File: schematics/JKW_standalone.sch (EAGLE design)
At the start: 173 parts, among them IC1 4093D, IC2 AT-MEGA-8, IC4 ATMEGA2560-16AU, T1 Farnell: 1299313, T2 Farnell: 1299313, T3 Farnell: 1299313, T4 T-IRLMS6702, T5 Farnell: 1299313

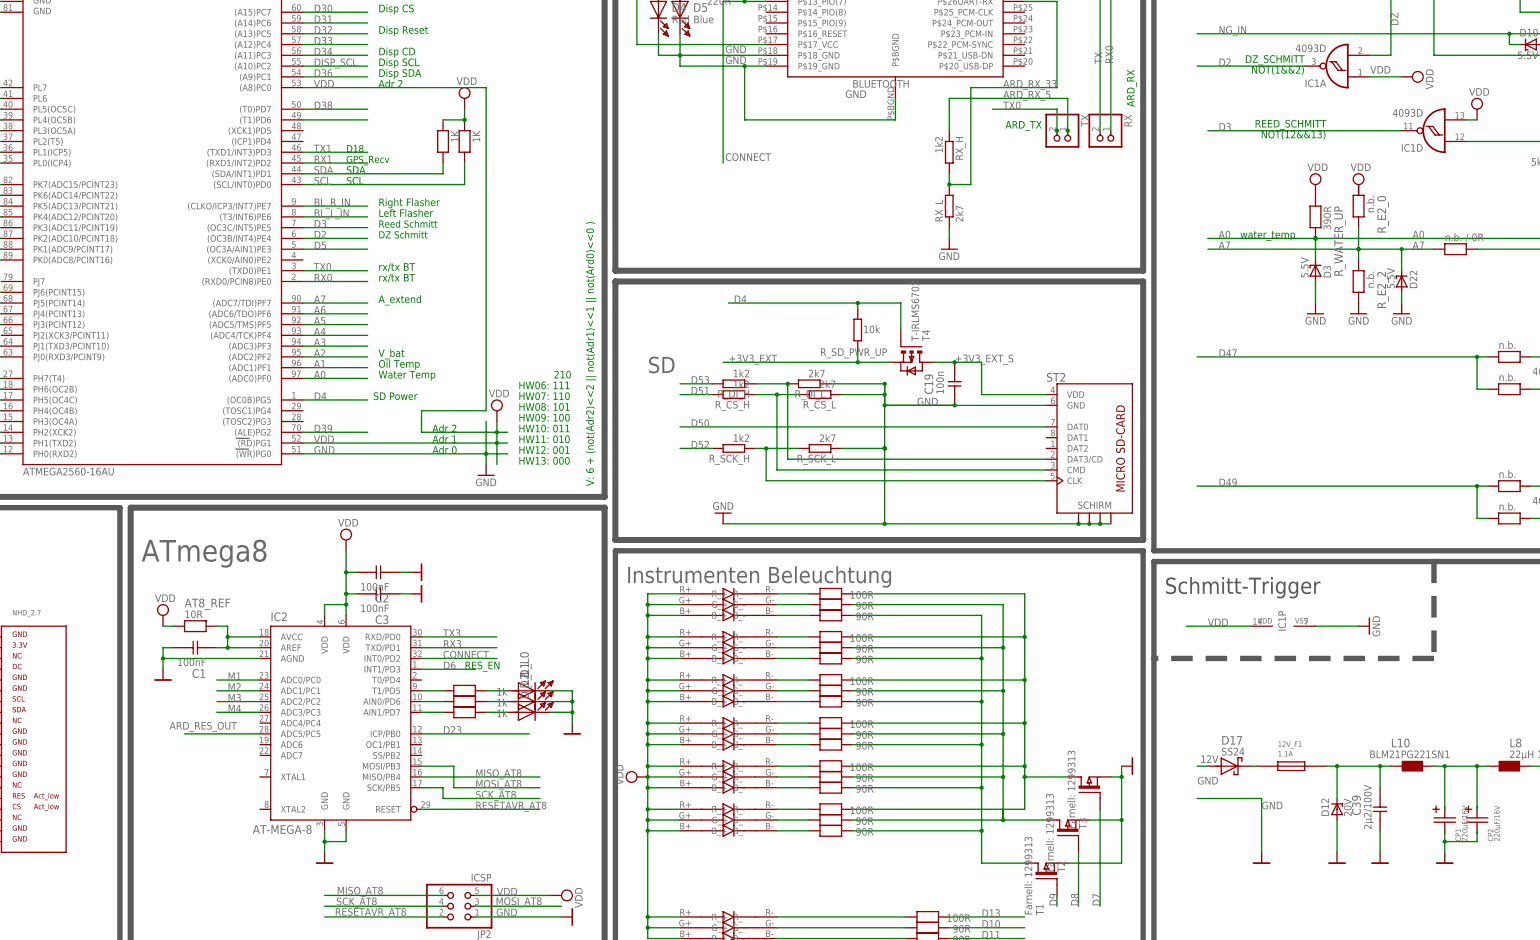
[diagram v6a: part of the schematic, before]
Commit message: Added detection of empty bat
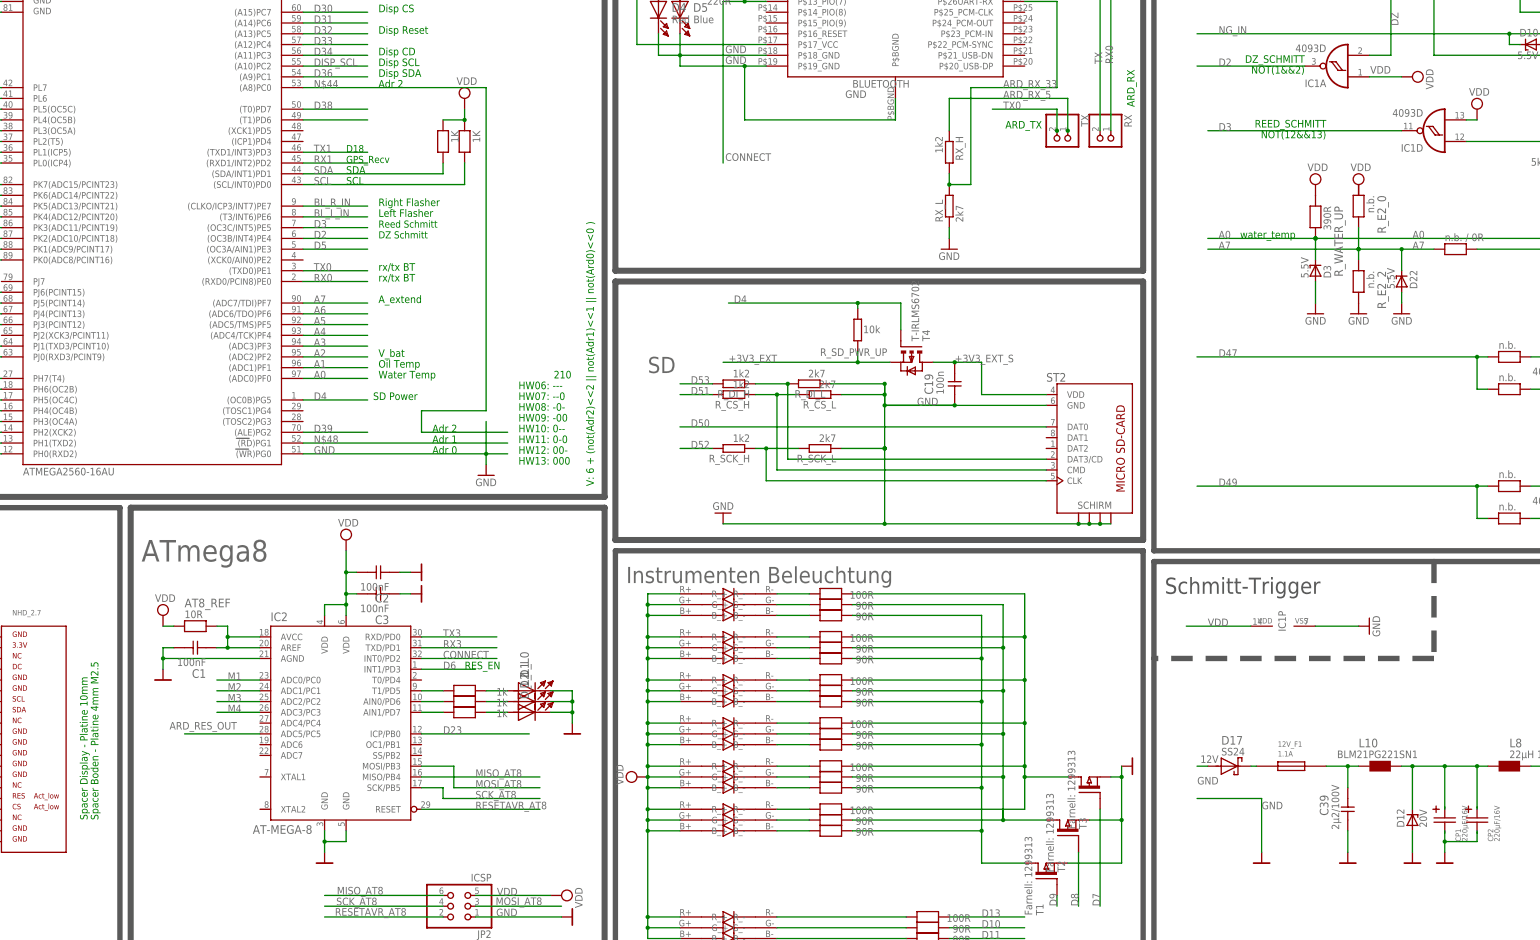
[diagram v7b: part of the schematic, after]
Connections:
- new net N$44: IC4.(A8)PC0
- new net N$48: IC4.(RD)PG1
- net 12V_SAFE: no longer D12.C
- net N$1: now also D12.C
- net VDD: no longer IC4.(A8)PC0, IC4.(RD)PG1
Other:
- note added: "HW06: ---"
- note added: "HW07: --0"
- note added: "HW08: -0-"
- note added: "HW09: -00"
- note added: "HW10: 0--"
- note added: "HW11: 0-0"
- note added: "HW12: 00-"
- note added: "Spacer Boden - Platine 4mm M2.5"
- note added: "Spacer Display - Platine 10mm"
- note removed: "HW06: 111"
- note removed: "HW07: 110"
- note removed: "HW08: 101"
- note removed: "HW09: 100"
- note removed: "HW10: 011"
- note removed: "HW11: 010"
- note removed: "HW12: 001"
- moved on the sheet: C39, D12, L10
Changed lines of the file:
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@@
 <?xml version="1.0" encoding="utf-8"?>
 <!DOCTYPE eagle SYSTEM "eagle.dtd">
-<eagle version="6.1">
+<eagle version="6.2">
 <drawing>
 <settings>
@@
 <part name="GND29" library="SparkFun" deviceset="GND" device=""/>
 <part name="SUPPLY20" library="supply2" deviceset="VDD" device=""/>
-<part name="SUPPLY21" library="supply2" deviceset="VDD" device=""/>
 <part name="GND32" library="SparkFun" deviceset="GND" device=""/>
 <part name="B_RIGHT" library="Kolja" deviceset="SMD_TASTER_MIT_KAPPE" device=""/>
@@
 <wire x1="322.58" y1="30.48" x2="403.86" y2="30.48" width="1.27" layer="97"/>
 <text x="325.12" y="55.88" size="3.81" layer="95">HW Adr</text>
-<text x="-134.62" y="104.14" size="1.778" layer="91">HW06: 111</text>
-<text x="-134.62" y="101.6" size="1.778" layer="91">HW07: 110</text>
-<text x="-134.62" y="99.06" size="1.778" layer="91">HW08: 101</text>
-<text x="-134.62" y="96.52" size="1.778" layer="91">HW09: 100</text>
-<text x="-134.62" y="93.98" size="1.778" layer="91">HW10: 011</text>
-<text x="-134.62" y="91.44" size="1.778" layer="91">HW11: 010</text>
-<text x="-134.62" y="88.9" size="1.778" layer="91">HW12: 001</text>
+<text x="-134.62" y="104.14" size="1.778" layer="91">HW06: ---</text>
+<text x="-134.62" y="101.6" size="1.778" layer="91">HW07: --0</text>
+<text x="-134.62" y="99.06" size="1.778" layer="91">HW08: -0-</text>
+<text x="-134.62" y="96.52" size="1.778" layer="91">HW09: -00</text>
+<text x="-134.62" y="93.98" size="1.778" layer="91">HW10: 0--</text>
+<text x="-134.62" y="91.44" size="1.778" layer="91">HW11: 0-0</text>
+<text x="-134.62" y="88.9" size="1.778" layer="91">HW12: 00-</text>
 <text x="-134.62" y="86.36" size="1.778" layer="91">HW13: 000</text>
 <text x="-116.84" y="81.28" size="1.778" layer="91" rot="R90">V: 6 + (not(Adr2)&lt;&lt;2 || not(Adr1)&lt;&lt;1 || not(Ard0)&lt;&lt;0 )</text>
 <text x="-127" y="106.68" size="1.778" layer="91"> 210</text>
 <text x="-154.94" y="93.98" size="1.778" layer="91">Adr 2</text>
+<text x="-236.22" y="2.54" size="1.778" layer="91" rot="R90">Spacer Display - Platine 10mm</text>
+<text x="-233.68" y="2.54" size="1.778" layer="91" rot="R90">Spacer Boden - Platine 4mm M2.5</text>
 </plain>
 <instances>
@@
 <attribute name="VALUE" x="99.06" y="17.145" size="1.778" layer="96"/>
 </instance>
-<instance part="C39" gate="C" x="68.58" y="5.08" smashed="yes" rot="MR270">
-<attribute name="NAME" x="61.976" y="3.556" size="2.032" layer="95" rot="MR90"/>
-<attribute name="VALUE" x="64.77" y="0.254" size="1.778" layer="96" rot="MR90"/>
-</instance>
-<instance part="U$408" gate="G$1" x="68.58" y="-7.62" smashed="yes"/>
-<instance part="L10" gate="G$1" x="76.2" y="15.24" smashed="yes">
-<attribute name="NAME" x="71.12" y="19.685" size="2.032" layer="95"/>
-<attribute name="VALUE" x="66.04" y="17.145" size="1.778" layer="96"/>
+<instance part="C39" gate="C" x="60.96" y="5.08" smashed="yes" rot="MR270">
+<attribute name="NAME" x="54.356" y="3.556" size="2.032" layer="95" rot="MR90"/>
+<attribute name="VALUE" x="57.15" y="0.254" size="1.778" layer="96" rot="MR90"/>
+</instance>
+<instance part="U$408" gate="G$1" x="60.96" y="-7.62" smashed="yes"/>
+<instance part="L10" gate="G$1" x="68.58" y="15.24" smashed="yes">
+<attribute name="NAME" x="63.5" y="19.685" size="2.032" layer="95"/>
+<attribute name="VALUE" x="58.42" y="17.145" size="1.778" layer="96"/>
 </instance>
 <instance part="U$210" gate="G$1" x="83.82" y="-7.62" smashed="yes"/>
-<instance part="U$159" gate="G$1" x="58.42" y="-7.62" smashed="yes"/>
+<instance part="U$159" gate="G$1" x="76.2" y="-7.62" smashed="yes"/>
 <instance part="U$161" gate="G$1" x="40.64" y="-7.62" smashed="yes"/>
 <instance part="GND4" gate="1" x="-294.64" y="177.8"/>
@@
 <instance part="D8" gate="G$1" x="111.76" y="236.22" rot="R270"/>
 <instance part="D9" gate="G$1" x="368.3" y="119.38" rot="R180"/>
-<instance part="D12" gate="G$1" x="58.42" y="5.08" rot="R90"/>
+<instance part="D12" gate="G$1" x="76.2" y="2.54" rot="R90"/>
 <instance part="SUPPLY11" gate="G$1" x="109.22" y="175.26"/>
 <instance part="R_REED_UP" gate="G$1" x="109.22" y="167.64" smashed="yes" rot="R270">
@@
 <instance part="GND29" gate="1" x="365.76" y="40.64"/>
 <instance part="SUPPLY20" gate="G$1" x="368.3" y="55.88"/>
-<instance part="SUPPLY21" gate="G$1" x="-139.7" y="99.06"/>
 <instance part="GND32" gate="1" x="-142.24" y="83.82"/>
 <instance part="B_RIGHT" gate="G$1" x="356" y="188"/>
@@
 </segment>
 <segment>
-<wire x1="58.42" y1="-5.08" x2="58.42" y2="2.54" width="0.1524" layer="91"/>
+<wire x1="76.2" y1="-5.08" x2="76.2" y2="0" width="0.1524" layer="91"/>
 <pinref part="U$159" gate="G$1" pin="GND"/>
 <pinref part="D12" gate="G$1" pin="A"/>
@@
 </segment>
 <segment>
-<wire x1="68.58" y1="0" x2="68.58" y2="-5.08" width="0.1524" layer="91"/>
+<wire x1="60.96" y1="0" x2="60.96" y2="-5.08" width="0.1524" layer="91"/>
 <pinref part="C39" gate="C" pin="2"/>
 <pinref part="U$408" gate="G$1" pin="GND"/>
@@
 <wire x1="368.3" y1="48.26" x2="378.46" y2="48.26" width="0.1524" layer="91"/>
 </segment>
-<segment>
-<pinref part="SUPPLY21" gate="G$1" pin="VDD"/>
-<wire x1="-139.7" y1="96.52" x2="-139.7" y2="93.98" width="0.1524" layer="91"/>
-<label x="-182.88" y="91.44" size="1.778" layer="95"/>
-<pinref part="IC4" gate="1" pin="(RD)PG1"/>
-<wire x1="-139.7" y1="93.98" x2="-139.7" y2="91.44" width="0.1524" layer="91"/>
-<wire x1="-139.7" y1="91.44" x2="-139.7" y2="86.36" width="0.1524" layer="91"/>
-<wire x1="-185.42" y1="91.44" x2="-139.7" y2="91.44" width="0.1524" layer="91"/>
-<junction x="-139.7" y="91.44"/>
-<wire x1="-139.7" y1="91.44" x2="-137.16" y2="91.44" width="0.1524" layer="91"/>
-<label x="-182.88" y="175.26" size="1.778" layer="95"/>
-<pinref part="IC4" gate="1" pin="(A8)PC0"/>
-<wire x1="-185.42" y1="175.26" x2="-142.24" y2="175.26" width="0.1524" layer="91"/>
-<wire x1="-142.24" y1="175.26" x2="-142.24" y2="99.06" width="0.1524" layer="91"/>
-<wire x1="-142.24" y1="99.06" x2="-157.48" y2="99.06" width="0.1524" layer="91"/>
-<wire x1="-157.48" y1="99.06" x2="-157.48" y2="93.98" width="0.1524" layer="91"/>
-<wire x1="-157.48" y1="93.98" x2="-139.7" y2="93.98" width="0.1524" layer="91"/>
-<junction x="-139.7" y="93.98"/>
-<wire x1="-139.7" y1="93.98" x2="-137.16" y2="93.98" width="0.1524" layer="91"/>
-</segment>
 </net>
 <net name="CONNECT" class="0">
@@
 <net name="N$1" class="0">
 <segment>
-<wire x1="81.28" y1="15.24" x2="83.82" y2="15.24" width="0.1524" layer="91"/>
+<wire x1="73.66" y1="15.24" x2="76.2" y2="15.24" width="0.1524" layer="91"/>
+<wire x1="76.2" y1="15.24" x2="83.82" y2="15.24" width="0.1524" layer="91"/>
 <wire x1="83.82" y1="15.24" x2="91.44" y2="15.24" width="0.1524" layer="91"/>
 <wire x1="91.44" y1="15.24" x2="93.98" y2="15.24" width="0.1524" layer="91"/>
@@
 <junction x="83.82" y="15.24"/>
 <junction x="91.44" y="15.24"/>
+<pinref part="D12" gate="G$1" pin="C"/>
+<wire x1="76.2" y1="5.08" x2="76.2" y2="15.24" width="0.1524" layer="91"/>
+<junction x="76.2" y="15.24"/>
 </segment>
 </net>
 <net name="12V_SAFE" class="0">
 <segment>
-<wire x1="68.58" y1="15.24" x2="71.12" y2="15.24" width="0.1524" layer="91"/>
-<wire x1="68.58" y1="10.16" x2="68.58" y2="15.24" width="0.1524" layer="91"/>
-<wire x1="58.42" y1="15.24" x2="68.58" y2="15.24" width="0.1524" layer="91"/>
-<wire x1="58.42" y1="7.62" x2="58.42" y2="15.24" width="0.1524" layer="91"/>
-<wire x1="55.88" y1="15.24" x2="58.42" y2="15.24" width="0.1524" layer="91"/>
-<junction x="68.58" y="15.24"/>
-<junction x="58.42" y="15.24"/>
+<wire x1="60.96" y1="15.24" x2="63.5" y2="15.24" width="0.1524" layer="91"/>
+<wire x1="60.96" y1="10.16" x2="60.96" y2="15.24" width="0.1524" layer="91"/>
+<wire x1="55.88" y1="15.24" x2="60.96" y2="15.24" width="0.1524" layer="91"/>
+<junction x="60.96" y="15.24"/>
 <pinref part="L10" gate="G$1" pin="1"/>
 <pinref part="C39" gate="C" pin="1"/>
 <pinref part="12V_F1" gate="G$1" pin="P$2"/>
-<pinref part="D12" gate="G$1" pin="C"/>
 </segment>
 </net>
@@
 </segment>
 </net>
+<net name="N$44" class="0">
+<segment>
+<label x="-182.88" y="175.26" size="1.778" layer="95"/>
+<pinref part="IC4" gate="1" pin="(A8)PC0"/>
+<wire x1="-185.42" y1="175.26" x2="-142.24" y2="175.26" width="0.1524" layer="91"/>
+<wire x1="-142.24" y1="175.26" x2="-142.24" y2="99.06" width="0.1524" layer="91"/>
+<wire x1="-142.24" y1="99.06" x2="-157.48" y2="99.06" width="0.1524" layer="91"/>
+<wire x1="-157.48" y1="99.06" x2="-157.48" y2="93.98" width="0.1524" layer="91"/>
+<wire x1="-157.48" y1="93.98" x2="-137.16" y2="93.98" width="0.1524" layer="91"/>
+</segment>
+</net>
+<net name="N$48" class="0">
+<segment>
+<pinref part="IC4" gate="1" pin="(RD)PG1"/>
+<wire x1="-185.42" y1="91.44" x2="-137.16" y2="91.44" width="0.1524" layer="91"/>
+<label x="-182.88" y="91.44" size="1.778" layer="95"/>
+</segment>
+</net>

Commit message: Board design: try to free interrupt inputs
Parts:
- added C10, C12, C13, C14, C15, C16, C17, C20, C21, C22, C23, C24, C25, C26, C27, C28, C29, C30: 100nF, RCLDT:C0805
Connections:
- new net N$49: IC4.PJ2(XCK3/PCINT11)
- net BLUE_INSTR: now also C12.2, C13.2, C14.2, C15.2, C16.2, C17.2
- net GND: now also C10.1, C12.1, C13.1, C14.1, C15.1, C16.1, C17.1, C20.1, C21.1, C22.1, C23.1, C24.1, C25.1, C26.1, C27.1, C28.1, C29.1, C30.1
- net GREEN_INSTR: now also C10.2, C20.2, C21.2, C22.2, C23.2, C24.2
- net RED_INSTR: now also C25.2, C26.2, C27.2, C28.2, C29.2, C30.2
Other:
- note removed: "HW Adr"
